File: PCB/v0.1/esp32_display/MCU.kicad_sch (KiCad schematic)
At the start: 15 parts, among them J2 Conn_01x06_Male, SW1 RST_BTN, SW2 SCREEN_OFF_BTN, U1 ESP32-WROOM-32

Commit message: Add housing edge, generate output files
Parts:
- added J3: External button, Connector_PinHeader_2.54mm:PinHeader_1x02_P2.54mm_Vertical, symbol Connector:Conn_01x02_Male
- J2: footprint Connector_PinHeader_2.54mm:PinHeader_1x06_P2.54mm_Vertical -> Connector_PinHeader_2.54mm:PinHeader_1x06_P2.54mm_Horizontal
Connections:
- net GND: now also J3.1 (Pin_1)
- net SCREEN_OFF_BTN: now also J3.2 (Pin_2)
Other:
- note added: "Connector in case button is off the PCB"
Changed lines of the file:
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@@
-    (stroke (width 0) (type default) (color 0 0 0 0))
-  )
-  (wire (pts (xy 79.375 165.735) (xy 79.375 166.37))
     (stroke (width 0) (type default) (color 0 0 0 0))
   )
@@
     (stroke (width 0) (type default) (color 0 0 0 0))
   )
+  (wire (pts (xy 87.63 174.625) (xy 87.63 179.07))
+    (stroke (width 0) (type default) (color 0 0 0 0))
+  )
   (bus (pts (xy 247.65 41.91) (xy 247.65 44.45))
     (stroke (width 0) (type default) (color 0 0 0 0))
@@
     (stroke (width 0) (type default) (color 0 0 0 0))
   )
+  (wire (pts (xy 87.63 166.37) (xy 87.63 172.085))
+    (stroke (width 0) (type default) (color 0 0 0 0))
+  )
   (wire (pts (xy 17.78 30.48) (xy 33.02 30.48))
     (stroke (width 0) (type default) (color 0 0 0 0))
@@
     (stroke (width 0) (type default) (color 0 0 0 0))
   )
-  (wire (pts (xy 79.375 166.37) (xy 60.96 166.37))
+  (wire (pts (xy 60.96 166.37) (xy 87.63 166.37))
     (stroke (width 0) (type default) (color 0 0 0 0))
   )
@@
     (stroke (width 0) (type default) (color 0 0 0 0))
   )
+  (wire (pts (xy 87.63 179.07) (xy 60.96 179.07))
+    (stroke (width 0) (type default) (color 0 0 0 0))
+  )
   (wire (pts (xy 156.21 97.79) (xy 172.72 97.79))
     (stroke (width 0) (type default) (color 0 0 0 0))
@@
   )
   (text "VDD: 3.0 - 3.6 V" (at 114.3 29.21 0)
+    (effects (font (size 1.27 1.27)) (justify left bottom))
+  )
+  (text "Connector in case button is off the PCB" (at 88.9 179.07 0)
     (effects (font (size 1.27 1.27)) (justify left bottom))
   )
@@
     (pin "1")
   )
+  (symbol (lib_id "Connector:Conn_01x02_Male") (at 92.71 174.625 180) (unit 1)
+    (in_bom yes) (on_board yes) (fields_autoplaced)
+    (property "Reference" "J3" (id 0) (at 93.98 172.0849 0)
+      (effects (font (size 1.27 1.27)) (justify right))
+    )
+    (property "Value" "External button" (id 1) (at 93.98 174.6249 0)
+      (effects (font (size 1.27 1.27)) (justify right))
+    )
+    (property "Footprint" "Connector_PinHeader_2.54mm:PinHeader_1x02_P2.54mm_Vertical" (id 2) (at 92.71 174.625 0)
+      (effects (font (size 1.27 1.27)) hide)
+    )
+    (property "Datasheet" "~" (id 3) (at 92.71 174.625 0)
+      (effects (font (size 1.27 1.27)) hide)
+    )
+    (pin "1")
+    (pin "2")
+  )
   (symbol (lib_id "Device:C") (at 13.97 173.355 0) (unit 1)
     (in_bom yes) (on_board yes) (fields_autoplaced)
@@
       (effects (font (size 1.27 1.27)) (justify right))
     )
-    (property "Footprint" "Connector_PinHeader_2.54mm:PinHeader_1x06_P2.54mm_Vertical" (id 2) (at 259.08 142.875 0)
-      (effects (font (size 1.27 1.27)) hide)
-    )
+    (property "Footprint" "Connector_PinHeader_2.54mm:PinHeader_1x06_P2.54mm_Horizontal" (id 2) (at 259.08 142.875 0)
+      (effects (font (size 1.27 1.27)) hide)
+    )

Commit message: Smaller footprint, no housing, right angle buttons
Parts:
- removed J3: External button, Connector_PinHeader_2.54mm:PinHeader_1x02_P2.54mm_Vertical, symbol Connector:Conn_01x02_Male
- SW1, SW2: footprint myLib:SW_SPST_PTS810 -> Button_Switch_THT:SW_Tactile_SPST_Angled_PTS645Vx83-2LFS
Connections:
- net TOUCH.IRQ: now also U1.27 (IO16); no longer U1.10 (IO25)
- net SCREEN_OFF_BTN renamed SCRN_OFF_BTN
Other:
- note removed: "Connector in case button is off the PCB"
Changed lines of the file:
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@@
   (no_connect (at 156.21 64.77))
   (no_connect (at 156.21 110.49))
+  (no_connect (at 156.21 102.87))
   (no_connect (at 125.73 90.17))
-  (no_connect (at 156.21 85.09))
   (no_connect (at 125.73 64.77))
   (no_connect (at 156.21 69.85))
@@
     (stroke (width 0) (type default) (color 0 0 0 0))
   )
-  (wire (pts (xy 156.21 107.95) (xy 175.26 107.95))
+  (wire (pts (xy 156.21 107.95) (xy 172.72 107.95))
     (stroke (width 0) (type default) (color 0 0 0 0))
   )
@@
     (stroke (width 0) (type default) (color 0 0 0 0))
   )
-  (wire (pts (xy 87.63 174.625) (xy 87.63 179.07))
-    (stroke (width 0) (type default) (color 0 0 0 0))
-  )
   (bus (pts (xy 247.65 41.91) (xy 247.65 44.45))
     (stroke (width 0) (type default) (color 0 0 0 0))
@@
     (stroke (width 0) (type default) (color 0 0 0 0))
   )
+  (wire (pts (xy 156.21 85.09) (xy 172.72 85.09))
+    (stroke (width 0) (type default) (color 0 0 0 0))
+  )
   (wire (pts (xy 245.11 66.04) (xy 228.6 66.04))
     (stroke (width 0) (type default) (color 0 0 0 0))
@@
     (stroke (width 0) (type default) (color 0 0 0 0))
   )
-  (wire (pts (xy 87.63 166.37) (xy 87.63 172.085))
-    (stroke (width 0) (type default) (color 0 0 0 0))
-  )
   (wire (pts (xy 17.78 30.48) (xy 33.02 30.48))
     (stroke (width 0) (type default) (color 0 0 0 0))
@@
     (stroke (width 0) (type default) (color 0 0 0 0))
   )
-  (wire (pts (xy 60.96 166.37) (xy 60.96 165.1))
+  (wire (pts (xy 60.96 165.1) (xy 60.96 166.37))
     (stroke (width 0) (type default) (color 0 0 0 0))
   )
@@
     (stroke (width 0) (type default) (color 0 0 0 0))
   )
-  (wire (pts (xy 60.96 166.37) (xy 87.63 166.37))
-    (stroke (width 0) (type default) (color 0 0 0 0))
-  )
   (wire (pts (xy 251.46 126.365) (xy 251.46 125.095))
     (stroke (width 0) (type default) (color 0 0 0 0))
@@
     (stroke (width 0) (type default) (color 0 0 0 0))
   )
-  (wire (pts (xy 87.63 179.07) (xy 60.96 179.07))
-    (stroke (width 0) (type default) (color 0 0 0 0))
-  )
   (wire (pts (xy 156.21 97.79) (xy 172.72 97.79))
     (stroke (width 0) (type default) (color 0 0 0 0))
@@
     (stroke (width 0) (type default) (color 0 0 0 0))
   )
+  (wire (pts (xy 79.375 166.37) (xy 60.96 166.37))
+    (stroke (width 0) (type default) (color 0 0 0 0))
+  )
   (wire (pts (xy 13.97 178.435) (xy 25.4 178.435))
     (stroke (width 0) (type default) (color 0 0 0 0))
   )
-  (wire (pts (xy 156.21 102.87) (xy 172.72 102.87))
-    (stroke (width 0) (type default) (color 0 0 0 0))
-  )
   (wire (pts (xy 156.21 74.93) (xy 172.72 74.93))
     (stroke (width 0) (type default) (color 0 0 0 0))
@@
     (effects (font (size 1.27 1.27)) (justify left bottom))
   )
-  (text "Connector in case button is off the PCB" (at 88.9 179.07 0)
-    (effects (font (size 1.27 1.27)) (justify left bottom))
-  )
   (label "UART_TX" (at 171.45 62.23 180)
     (effects (font (size 1.27 1.27)) (justify right bottom))
@@
     (effects (font (size 1.27 1.27)) (justify right bottom))
   )
-  (label "SCREEN_OFF_BTN" (at 79.375 166.37 180)
+  (label "SCRN_OFF_BTN" (at 79.375 166.37 180)
     (effects (font (size 1.27 1.27)) (justify right bottom))
   )
@@
     (effects (font (size 1.27 1.27)) (justify right bottom))
   )
+  (label "TOUCH.IRQ" (at 172.72 85.09 180)
+    (effects (font (size 1.27 1.27)) (justify right bottom))
+  )
   (label "TOUCH.SPI_CS" (at 228.6 66.04 0)
     (effects (font (size 1.27 1.27)) (justify left bottom))
@@
     (effects (font (size 1.27 1.27)) (justify left bottom))
   )
-  (label "TOUCH.IRQ" (at 172.72 102.87 180)
-    (effects (font (size 1.27 1.27)) (justify right bottom))
-  )
   (label "TOUCH.SPI_CS" (at 172.72 72.39 180)
     (effects (font (size 1.27 1.27)) (justify right bottom))
@@
     (effects (font (size 1.27 1.27)) (justify right bottom))
   )
-  (label "SCREEN_OFF_BTN" (at 175.26 107.95 180)
+  (label "SCRN_OFF_BTN" (at 172.72 107.95 180)
     (effects (font (size 1.27 1.27)) (justify right bottom))
   )
@@
     (property "Reference" "SW1" (id 0) (at 31.75 176.53 90))
     (property "Value" "RST_BTN" (id 1) (at 33.02 173.99 90))
-    (property "Footprint" "myLib:SW_SPST_PTS810" (id 2) (at 30.48 172.72 0)
+    (property "Footprint" "Button_Switch_THT:SW_Tactile_SPST_Angled_PTS645Vx83-2LFS" (id 2) (at 30.48 172.72 0)
       (effects (font (size 1.27 1.27)) hide)
     )
@@
     (property "Reference" "SW2" (id 0) (at 67.31 176.53 90))
     (property "Value" "SCREEN_OFF_BTN" (id 1) (at 73.66 173.99 90))
-    (property "Footprint" "myLib:SW_SPST_PTS810" (id 2) (at 66.04 172.72 0)
+    (property "Footprint" "Button_Switch_THT:SW_Tactile_SPST_Angled_PTS645Vx83-2LFS" (id 2) (at 66.04 172.72 0)
       (effects (font (size 1.27 1.27)) hide)
     )
@@
     (pin "1")
   )
-  (symbol (lib_id "Connector:Conn_01x02_Male") (at 92.71 174.625 180) (unit 1)
-    (in_bom yes) (on_board yes) (fields_autoplaced)
-    (property "Reference" "J3" (id 0) (at 93.98 172.0849 0)
-      (effects (font (size 1.27 1.27)) (justify right))
-    )
-    (property "Value" "External button" (id 1) (at 93.98 174.6249 0)
-      (effects (font (size 1.27 1.27)) (justify right))
-    )
-    (property "Footprint" "Connector_PinHeader_2.54mm:PinHeader_1x02_P2.54mm_Vertical" (id 2) (at 92.71 174.625 0)
-      (effects (font (size 1.27 1.27)) hide)
-    )
-    (property "Datasheet" "~" (id 3) (at 92.71 174.625 0)
-      (effects (font (size 1.27 1.27)) hide)
-    )
-    (pin "1")
-    (pin "2")
-  )
   (symbol (lib_id "Device:C") (at 13.97 173.355 0) (unit 1)

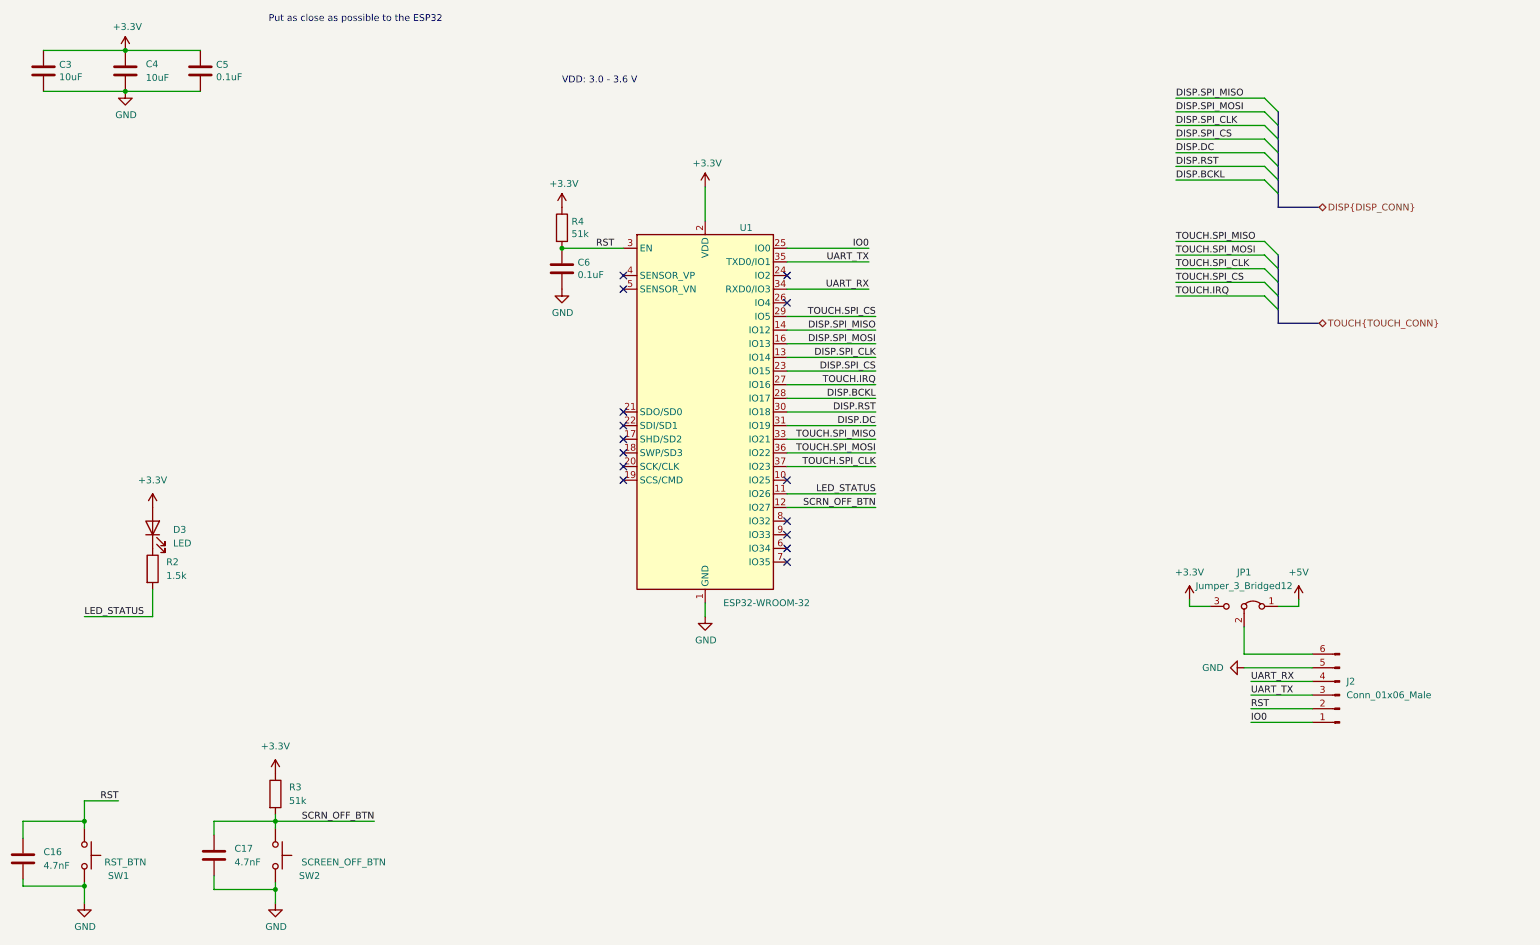
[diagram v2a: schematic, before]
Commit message: Add serial resistors to SPI lines (PCB not finished)
Still missing placment of RC filters.
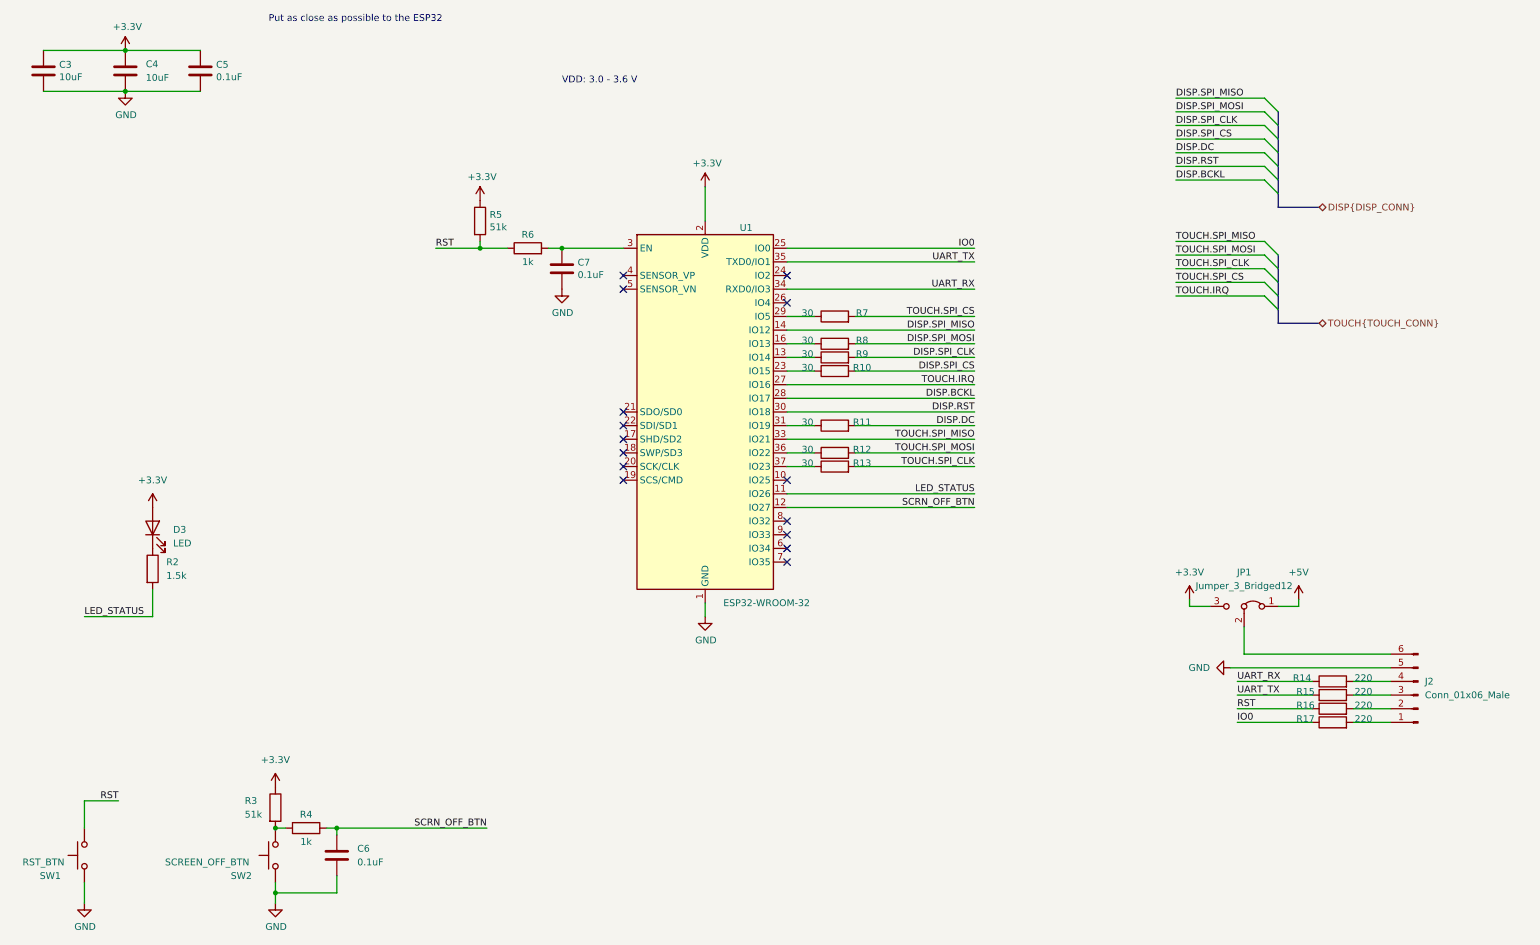
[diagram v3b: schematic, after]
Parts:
- removed C16, C17: 4.7nF, Capacitor_SMD:C_0603_1608Metric_Pad1.08x0.95mm_HandSolder, symbol Device:C
- added C6: 0.1uF, Capacitor_SMD:C_0603_1608Metric_Pad1.08x0.95mm_HandSolder, symbol Device:C
- added R10, R11, R12, R13, R7, R8, R9: 30, Resistor_SMD:R_0603_1608Metric_Pad0.98x0.95mm_HandSolder, symbol Device:R
- added R14, R15, R16, R17: 220, Resistor_SMD:R_0603_1608Metric_Pad0.98x0.95mm_HandSolder, symbol Device:R
- added R4, R6: 1k, Resistor_SMD:R_0603_1608Metric_Pad0.98x0.95mm_HandSolder, symbol Device:R
- renumbered C6 to C7, R4 to R5
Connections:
- net DISP.DC: now also R11.2; no longer U1.31 (IO19)
- net DISP.SPI_CLK: now also R9.2; no longer U1.13 (IO14)
- net DISP.SPI_CS: now also R10.2; no longer U1.23 (IO15)
- net DISP.SPI_MOSI: now also R8.2; no longer U1.16 (IO13)
- net GND: now also C6.2
- net IO0: now also R17.1; no longer J2.1 (Pin_1)
- net RST: now also R16.1, R6.1; no longer C7.1, J2.2 (Pin_2), U1.3 (EN)
- net SCRN_OFF_BTN: now also C6.1, R4.1; no longer R3.2, SW2.1
- net TOUCH.SPI_CLK: now also R13.2; no longer U1.37 (IO23)
- net TOUCH.SPI_CS: now also R7.2; no longer U1.29 (IO5)
- net TOUCH.SPI_MOSI: now also R12.2; no longer U1.36 (IO22)
- net UART_RX: now also R14.1; no longer J2.4 (Pin_4)
- net UART_TX: now also R15.1; no longer J2.3 (Pin_3)
- new net: R9.1, U1.13 (IO14)
- new net: R8.1, U1.16 (IO13)
- new net: R10.1, U1.23 (IO15)
- new net: R7.1, U1.29 (IO5)
- new net: C7.1, R6.2, U1.3 (EN)
- new net: R11.1, U1.31 (IO19)
- new net: R12.1, U1.36 (IO22)
- new net: R13.1, U1.37 (IO23)
- new net: R3.2, R4.2, SW2.1
- new net: J2.2 (Pin_2), R16.2
- new net: J2.1 (Pin_1), R17.2
- new net: J2.3 (Pin_3), R15.2
- new net: J2.4 (Pin_4), R14.2
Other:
- moved on the sheet: J2, R3, R5, SW1, SW2
